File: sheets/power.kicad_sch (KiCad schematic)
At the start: 18 parts, among them J3 USB_C_Receptacle_USB2.0_16P, J5 Power Select, U4 LMR51430XFDDCR, U6 USBLC6-2P6, U9 AMS1117-3.3

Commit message: added current rush limiting resistors to bmp581
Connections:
- net VCC renamed +3V3
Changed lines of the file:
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@@
-	)
-	(junction
-		(at 137.16 118.11)
-		(diameter 0)
-		(color 0 0 0 0)
 	)
 	(junction
@@
 	)
 	(junction
-		(at 137.16 135.89)
-		(diameter 0)
-		(color 0 0 0 0)
-	)
-	(junction
 		(at 214.63 128.27)
 		(diameter 0)
@@
 	(wire
 		(pts
-			(xy 129.54 118.11) (xy 137.16 118.11)
-		)
-		(stroke
-			(width 0)
-			(type default)
-		)
-	)
-	(wire
-		(pts
 			(xy 59.69 58.42) (xy 77.47 58.42)
 		)
@@
 		(pts
 			(xy 57.15 73.66) (xy 54.61 73.66)
-		)
-		(stroke
-			(width 0)
-			(type default)
-		)
-	)
-	(wire
-		(pts
-			(xy 129.54 135.89) (xy 137.16 135.89)
 		)
 		(stroke
@@
 		)
 		(instances
-			(project "nc_fc"
+			(project "aerolotl"
 				(path "/3f5bc5ea-feaa-4ed9-b0e0-c918b1fb5754/74cb3ba4-5441-4040-b144-f529fa281743"
 					(reference "U6")
@@
 		)
 		(instances
-			(project "nc_fc"
+			(project "aerolotl"
 				(path "/3f5bc5ea-feaa-4ed9-b0e0-c918b1fb5754/74cb3ba4-5441-4040-b144-f529fa281743"
 					(reference "#PWR028")
@@
 		)
 		(instances
-			(project "nc_fc"
+			(project "aerolotl"
 				(path "/3f5bc5ea-feaa-4ed9-b0e0-c918b1fb5754/74cb3ba4-5441-4040-b144-f529fa281743"
 					(reference "#PWR026")
@@
 		)
 		(instances
-			(project "nc_fc"
+			(project "aerolotl"
 				(path "/3f5bc5ea-feaa-4ed9-b0e0-c918b1fb5754/74cb3ba4-5441-4040-b144-f529fa281743"
 					(reference "#PWR027")
@@
 		)
 		(instances
-			(project "nc_fc"
+			(project "aerolotl"
 				(path "/3f5bc5ea-feaa-4ed9-b0e0-c918b1fb5754/74cb3ba4-5441-4040-b144-f529fa281743"
 					(reference "U9")
@@
 		)
 		(instances
-			(project "nc_fc"
+			(project "aerolotl"
 				(path "/3f5bc5ea-feaa-4ed9-b0e0-c918b1fb5754/74cb3ba4-5441-4040-b144-f529fa281743"
 					(reference "C26")
@@
 	)
 	(symbol
-		(lib_id "power:VCC")
-		(at 210.82 63.5 90)
-		(unit 1)
-		(exclude_from_sim no)
-		(in_bom yes)
-		(on_board yes)
-		(dnp no)
-		(fields_autoplaced yes)
-		(property "Reference" "#PWR038"
-			(at 214.63 63.5 0)
-			(effects
-				(font
-					(size 1.27 1.27)
-				)
-				(hide yes)
-			)
-		)
-		(property "Value" "VCC"
-			(at 207.01 63.4999 90)
-			(effects
-				(font
-					(size 1.27 1.27)
-				)
-				(justify left)
-			)
-		)
-		(property "Footprint" ""
-			(at 210.82 63.5 0)
-			(effects
-				(font
-					(size 1.27 1.27)
-				)
-				(hide yes)
-			)
-		)
-		(property "Datasheet" ""
-			(at 210.82 63.5 0)
-			(effects
-				(font
-					(size 1.27 1.27)
-				)
-				(hide yes)
-			)
-		)
-		(property "Description" "Power symbol creates a global label with name \"VCC\""
-			(at 210.82 63.5 0)
-			(effects
-				(font
-					(size 1.27 1.27)
-				)
-				(hide yes)
-			)
-		)
-		(pin "1"
-		)
-		(instances
-			(project "nc_fc"
-				(path "/3f5bc5ea-feaa-4ed9-b0e0-c918b1fb5754/74cb3ba4-5441-4040-b144-f529fa281743"
-					(reference "#PWR038")
-					(unit 1)
-				)
-			)
-		)
-	)
-	(symbol
 		(lib_id "Device:C")
 		(at 120.65 63.5 0)
@@
 		)
 		(instances
-			(project "nc_fc"
+			(project "aerolotl"
 				(path "/3f5bc5ea-feaa-4ed9-b0e0-c918b1fb5754/74cb3ba4-5441-4040-b144-f529fa281743"
 					(reference "C27")
@@
 		)
 		(instances
-			(project "nc_fc"
+			(project "aerolotl"
 				(path "/3f5bc5ea-feaa-4ed9-b0e0-c918b1fb5754/74cb3ba4-5441-4040-b144-f529fa281743"
 					(reference "#PWR029")
@@
 	)
 	(symbol
+		(lib_id "power:+3V3")
+		(at 210.82 63.5 90)
+		(unit 1)
+		(exclude_from_sim no)
+		(in_bom yes)
+		(on_board yes)
+		(dnp no)
+		(property "Reference" "#PWR038"
+			(at 214.63 63.5 0)
+			(effects
+				(font
+					(size 1.27 1.27)
+				)
+				(hide yes)
+			)
+		)
+		(property "Value" "+3V3"
+			(at 207.01 63.754 0)
+			(effects
+				(font
+					(size 1.27 1.27)
+				)
+			)
+		)
+		(property "Footprint" ""
+			(at 210.82 63.5 0)
+			(effects
+				(font
+					(size 1.27 1.27)
+				)
+				(hide yes)
+			)
+		)
+		(property "Datasheet" ""
+			(at 210.82 63.5 0)
+			(effects
+				(font
+					(size 1.27 1.27)
+				)
+				(hide yes)
+			)
+		)
+		(property "Description" "Power symbol creates a global label with name \"+3V3\""
+			(at 210.82 63.5 0)
+			(effects
+				(font
+					(size 1.27 1.27)
+				)
+				(hide yes)
+			)
+		)
+		(pin "1"
+		)
+		(instances
+			(project "aerolotl"
+				(path "/3f5bc5ea-feaa-4ed9-b0e0-c918b1fb5754/74cb3ba4-5441-4040-b144-f529fa281743"
+					(reference "#PWR038")
+					(unit 1)
+				)
+			)
+		)
+	)
+	(symbol
 		(lib_id "Device:R")
 		(at 62.23 63.5 90)
@@
 		)
 		(instances
-			(project "nc_fc"
+			(project "aerolotl"
 				(path "/3f5bc5ea-feaa-4ed9-b0e0-c918b1fb5754/74cb3ba4-5441-4040-b144-f529fa281743"
 					(reference "R5")
@@
 		)
 		(instances
-			(project "nc_fc"
+			(project "aerolotl"
 				(path "/3f5bc5ea-feaa-4ed9-b0e0-c918b1fb5754/74cb3ba4-5441-4040-b144-f529fa281743"
 					(reference "R6")
@@
 		)
 		(instances
-			(project "nc_fc"
+			(project "aerolotl"
 				(path "/3f5bc5ea-feaa-4ed9-b0e0-c918b1fb5754/74cb3ba4-5441-4040-b144-f529fa281743"
 					(reference "FB3")
@@
 		)
 		(instances
-			(project "nc_fc"
+			(project "aerolotl"
 				(path "/3f5bc5ea-feaa-4ed9-b0e0-c918b1fb5754/74cb3ba4-5441-4040-b144-f529fa281743"
 					(reference "J5")

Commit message: Fixed up power, added remaining to do
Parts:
- added J1, J7: Conn_01x02_Pin, symbol Connector:Conn_01x02_Pin
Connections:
- net GND: now also J1.2 (Pin_2)
- net +12V: now reaches Cin1.1, Cinx1.1, U4.3 (VIN), U4.5 (EN)
- net +12V: now also J1.1 (Pin_1), J7.1 (Pin_1)
- new net +12V_ARM: J7.2 (Pin_2)
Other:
- note removed: "To-do Reduce Battery voltage from 12V or whatever to 3V use TI schematic"

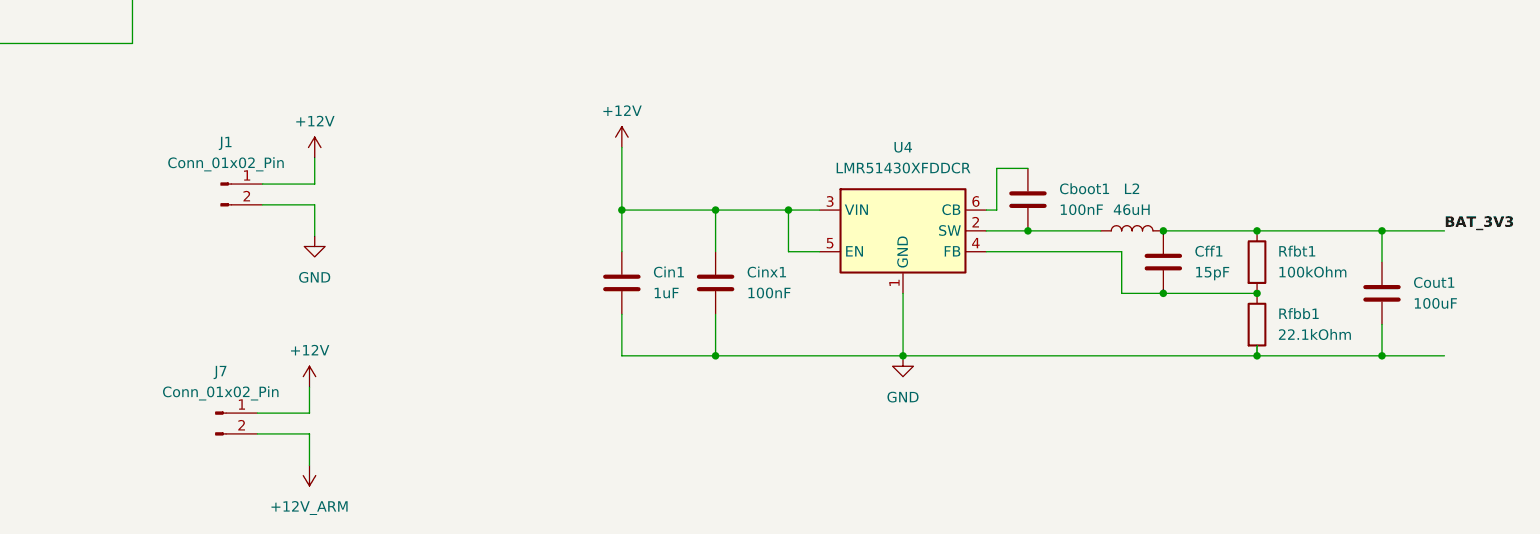
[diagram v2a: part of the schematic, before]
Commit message: polished up circuit, added new 16.8V to 7.4V step down circuit components
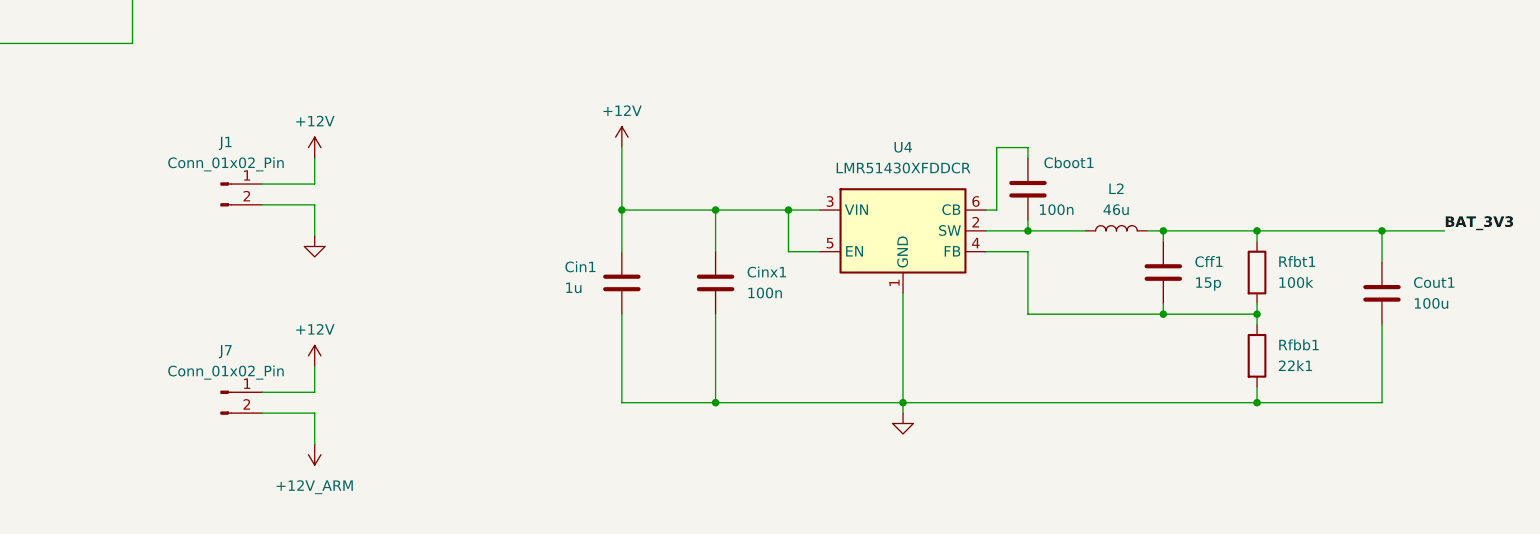
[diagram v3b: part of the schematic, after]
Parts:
- Cboot1, Cinx1: value 100nF -> 100n
- Cff1: value 15pF -> 15p
- Cin1: value 1uF -> 1u
- Cout1: value 100uF -> 100u
- L2: value 46uH -> 46u
- Rfbb1: value 22.1kOhm -> 22k1
- Rfbt1: value 100kOhm -> 100k
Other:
- moved on the sheet: Cboot1, Cff1, J7, L2, Rfbb1, Rfbt1

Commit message: second push
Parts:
- added C37: 2n2, symbol Device:C
- added C38: 15n, symbol Device:C
- added C39: 33n, symbol Device:C
- added C40: 100n, symbol Device:C
- added C41: 47u, symbol Device:C
- added Cin2: 10u, symbol Device:C
- added Cinx2: 4.7u, symbol Device:C
- added L3: 46u, symbol Device:L
- added Rcomp: 4k7, symbol Device:R
- added Renb: 36k, symbol Device:R
- added Rent: 100k, symbol Device:R
- added Rfbb: 10k, symbol Device:R
- added Rfbt: 82k5, symbol Device:R
- added Rt: 56k, symbol Device:R
- added U8: TPS54620RGYR, TPS54620RGYR:QFN50P350X350X100-15N, symbol aerolotl_custom:TPS54620RGYR
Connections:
- net +12V: now also Cin2.1, Cinx2.1, Rent.1, U8.4 (PVIN_4), U8.5 (PVIN_5), U8.6 (VIN)
- net GND: now also C37.2, C38.2, C39.2, C41.2, Cin2.2, Cinx2.2, Renb.2, Rfbb.2, Rt.2, U8.15 (EXP), U8.2 (GND_2), U8.3 (GND_3)
- new net: C39.1, Rcomp.1, U8.8 (COMP)
- new net: C38.1, Rcomp.2
- new net: C40.1, U8.13 (BOOT)
- new net: C40.2, L3.1, U8.11 (PH_11), U8.12 (PH_12)
- new net: Renb.1, Rent.2, U8.10 (EN)
- new net: Rfbb.1, Rfbt.2, U8.7 (VSENSE)
- new net: C37.1, U8.9 (SS/TR)
- new net: Rt.1, U8.1 (RT/CLK)
- new net +7V4_SERVO: C41.1, L3.2, Rfbt.1
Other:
- moved on the sheet: Cboot1, Cff1, Cin1, Cinx1, Cout1, J1, J5, J7, L2, Rfbb1, Rfbt1, U4

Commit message: added spi
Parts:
- added R15: 10k, symbol Device:R
- added R16: 3k3, symbol Device:R
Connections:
- net +12V: now also R15.1
- net GND: now also R16.2
- new net VOLT_SENSE: R15.2, R16.1
- no-connect marks 2 -> 3

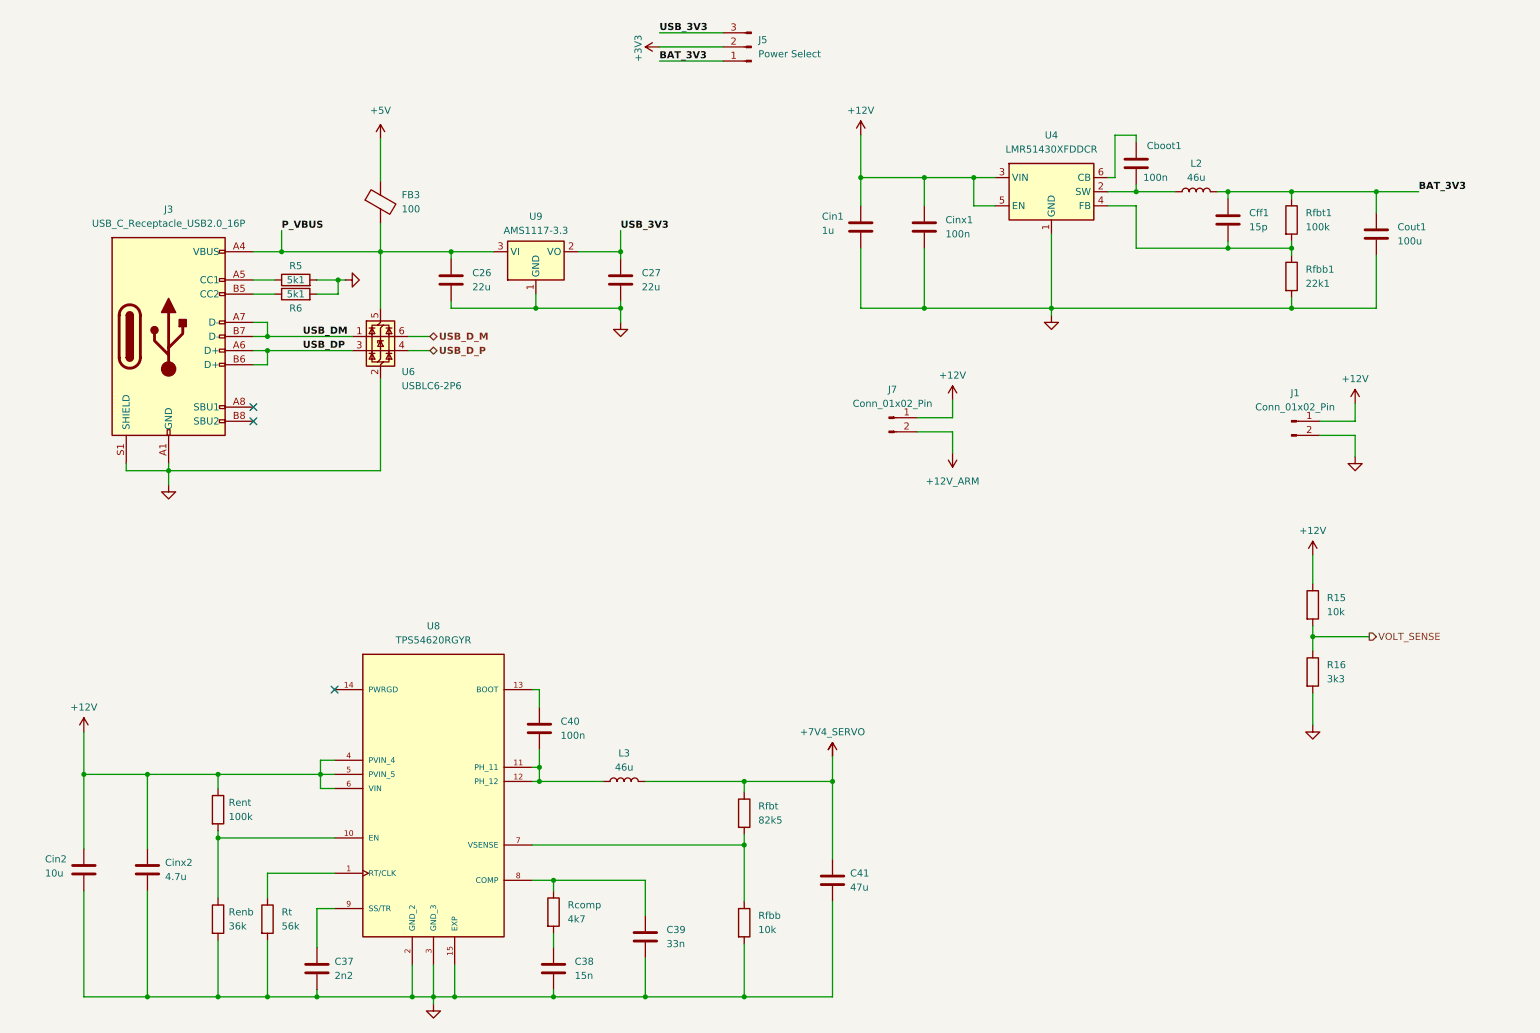
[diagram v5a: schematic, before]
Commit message: added gpio connections in root, UART8, ADC2
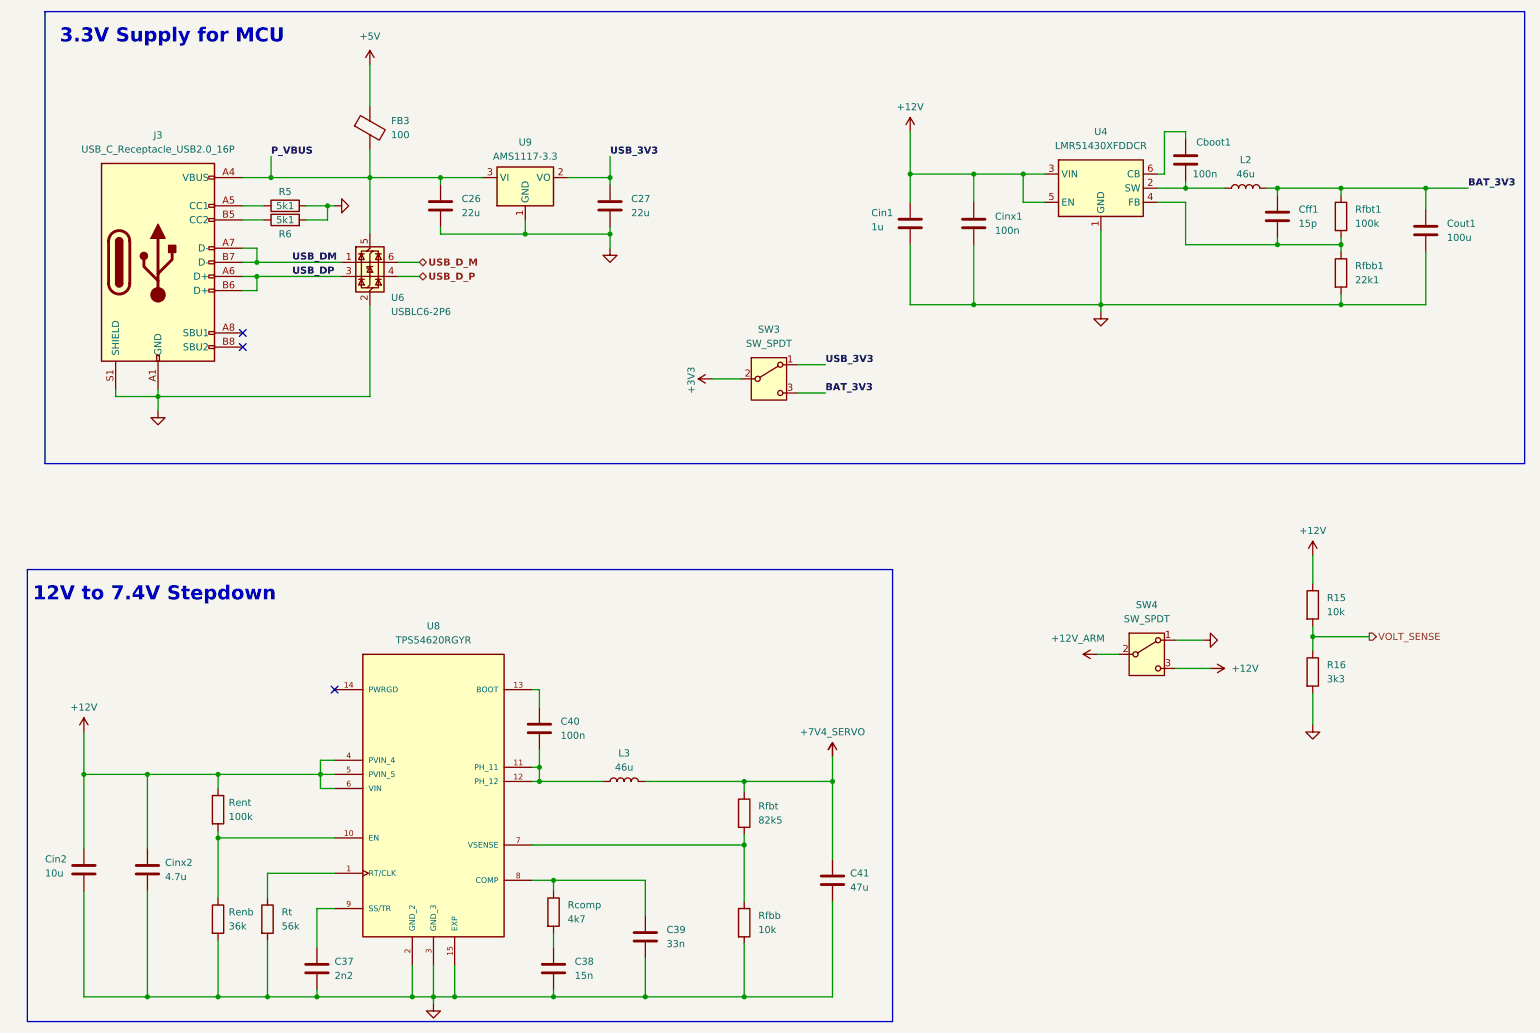
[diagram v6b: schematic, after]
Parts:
- removed J1, J7: Conn_01x02_Pin, symbol Connector:Conn_01x02_Pin
- removed J5: Power Select, symbol Connector:Conn_01x03_Pin
- added SW3, SW4: SW_SPDT, symbol Switch:SW_SPDT
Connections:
- net +12V: now also SW4.3 (C)
- net +12V_ARM: now also SW4.2 (B)
- net +3V3: now also SW3.2 (B)
- net BAT_3V3: now also SW3.3 (C)
- net GND: now also SW4.1 (A)
- net USB_3V3: now also SW3.1 (A)
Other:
- note added: "12V to 7.4V Stepdown"
- note added: "3.3V Supply for MCU"
- moved on the sheet: C26, C27, Cboot1, Cff1, Cin1, Cinx1, Cout1, FB3, J3, L2, R5, R6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

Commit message: Rev1 schematic done
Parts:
- removed Rcomp: 4k7, symbol Device:R
- removed SW4: SW_SPDT, symbol Switch:SW_SPDT
- removed U8: TPS54620RGYR, TPS54620RGYR:QFN50P350X350X100-15N, symbol aerolotl_custom:TPS54620RGYR
- added R10: R, symbol Device:R
- added SW4: SW_SPST, symbol Switch:SW_SPST
- added U3: TPS54620RGYR, TPS54620RGYR:QFN50P350X350X100-15N, symbol aerolotl_custom:TPS54620RGYR
- renumbered Cin2 to C28, Cinx2 to C29, C37 to C30, C26 to C31, C40 to C32, C38 to C33, C27 to C34, C39 to C35, C41 to C36, Cin1 to C37, Cinx1 to C38, Cboot1 to C39, Cff1 to C40, Cout1 to C41, FB3 to FB2, J3 to J2, L3 to L2, L2 to L3, Rfbt to R11, Rfbb to R12, R15 to R13, R16 to R14, Rfbt1 to R15, Rfbb1 to R16, Rent to R5, Renb to R6, Rt to R7, R5 to R8, R6 to R9, U6 to U2, U9 to U4, U4 to U5
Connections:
- net +12V: now also SW4.2 (B), U3.4 (PVIN_4), U3.5 (PVIN_5), U3.6 (VIN)
- net +12V_ARM: now also SW4.1 (A)
- net GND: now also U3.15 (EXP), U3.2 (GND_2), U3.3 (GND_3)
- net at C35.1: now also R10.1, U3.8 (COMP)
- net at C33.1: now also R10.2
- net at C32.1: now also U3.13 (BOOT)
- net at C32.2, L2.1: now also U3.11 (PH_11), U3.12 (PH_12)
- net at R5.2, R6.1: now also U3.10 (EN)
- net at R11.2, R12.1: now also U3.7 (VSENSE)
- net at C30.1: now also U3.9 (SS/TR)
- net at R7.1: now also U3.1 (RT/CLK)
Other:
- moved on the sheet: C28, C29, C30, C31, C32, C33, C34, C35, C36, C37, C38, C39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
